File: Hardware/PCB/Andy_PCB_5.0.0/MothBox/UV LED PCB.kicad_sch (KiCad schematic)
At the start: 24 parts, among them P4 External Attractor, Q10 BC817, Q11 BC817, Q8 BC817, Q9 BC817, U10 IRF9335TRPBF, U11 IRF9335TRPBF, U12 IRF9335TRPBF, U13 IRF9335TRPBF

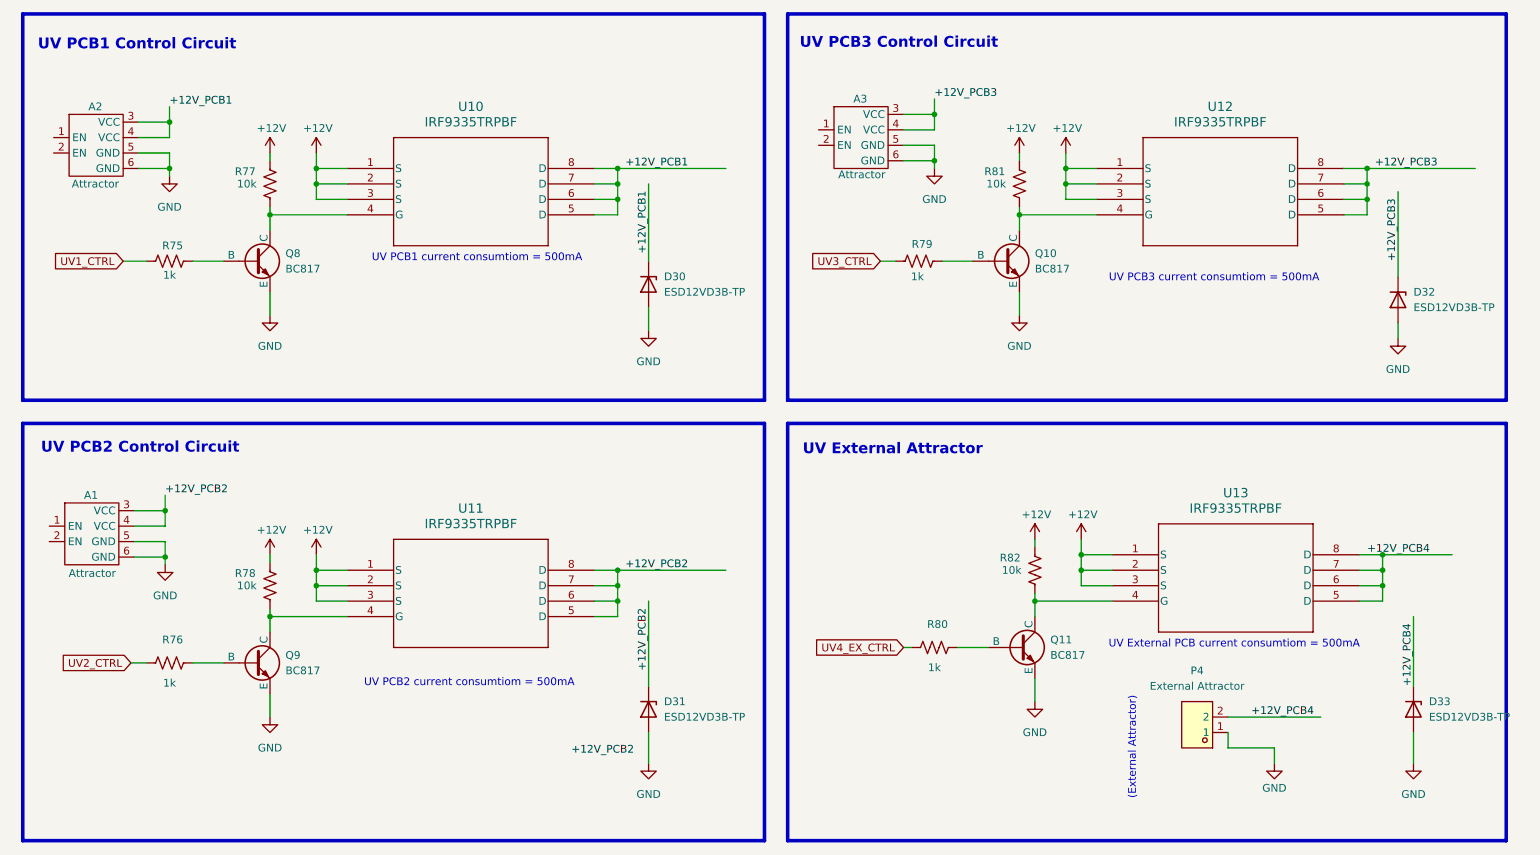
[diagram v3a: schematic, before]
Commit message: Tweaked Mothbeam and added GPS footprints
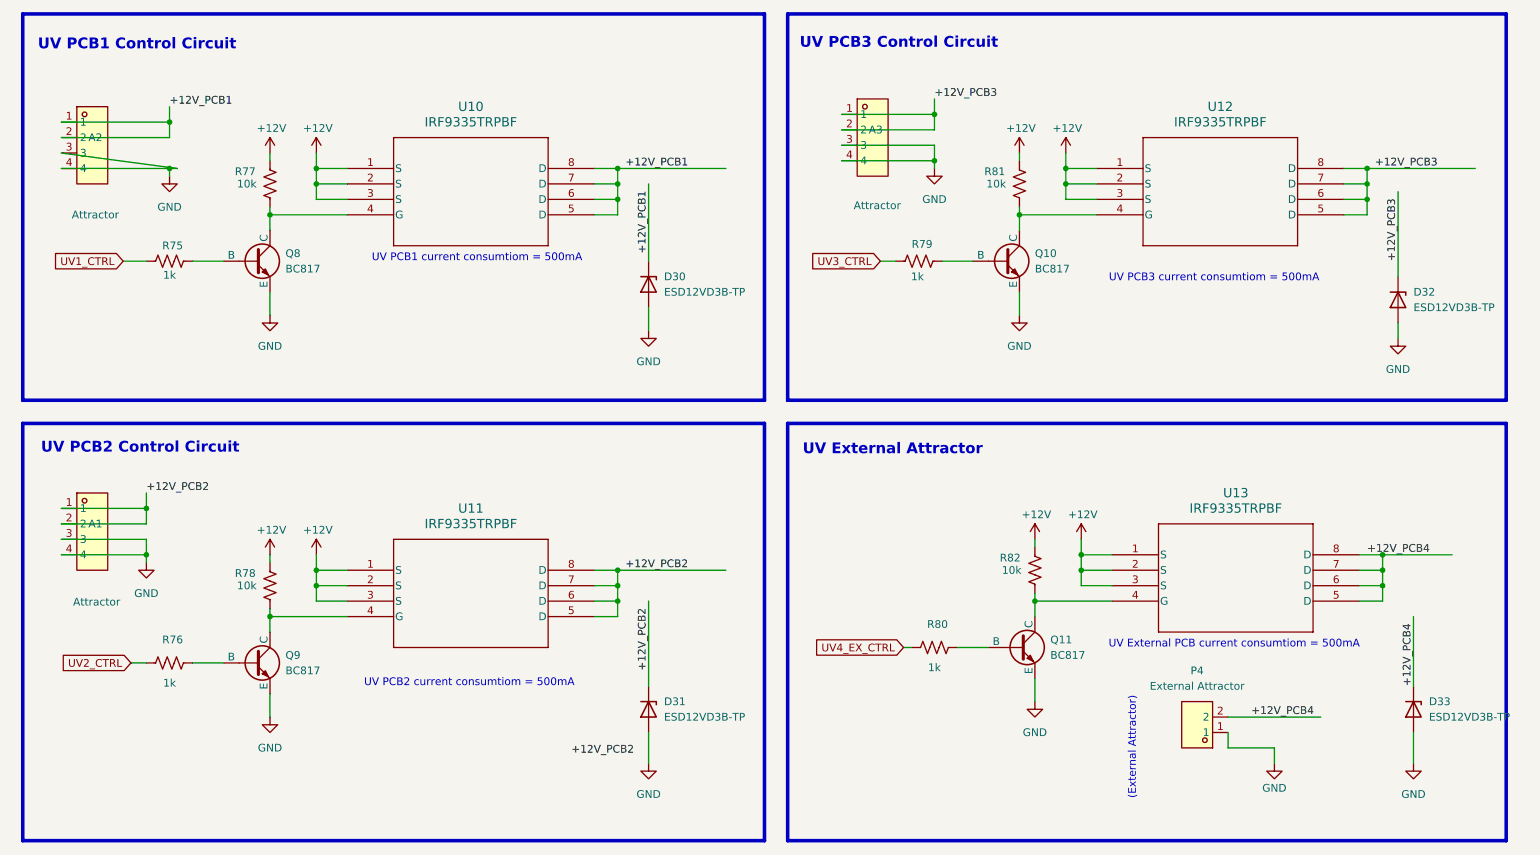
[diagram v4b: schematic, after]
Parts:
- A1, A2, A3: footprint Attractor:attractor -> Attractor:HDR-TH_4P-P2.54-H-M-W10.4; symbol attractor:Attractor_Module -> attractor_AQ:PZ254R-11-04P; LCSC Part (none) -> C492412
- P4: footprint easyeda2kicad:CONN-TH_DB301V-3.5-2P-GN -> easyeda2kicad:CONN-TH_2P-P5.08_DIBO_DB142R-5.08-2P; symbol easyeda2kicad:DB301V-3.5-2P-GN -> easyeda2kicad:DB142R-5.08-2P; LCSC Part C695629 -> C2898709
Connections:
- net +12V_PCB1: now also A2.1, A2.2; no longer A2.3 (VCC), A2.4 (VCC)
- net +12V_PCB2: now also A1.1, A1.2; no longer A1.3 (VCC), A1.4 (VCC)
- net +12V_PCB3: now also A3.1, A3.2; no longer A3.3 (VCC), A3.4 (VCC)
- net GND: now also A1.3, A1.4, A2.3, A2.4, A3.3, A3.4; no longer A1.5 (GND), A1.6 (GND), A2.5 (GND), A2.6 (GND), A3.5 (GND), A3.6 (GND)
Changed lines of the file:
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@@
 	)
 	(junction
-		(at 50.0835 109.5921)
+		(at 46.99 109.22)
 		(diameter 0)
 		(color 0 0 0 0)
@@
 	)
 	(junction
-		(at 50.0835 117.2121)
+		(at 46.99 116.84)
 		(diameter 0)
 		(color 0 0 0 0)
@@
 	(wire
 		(pts
-			(xy 50.0835 117.2121) (xy 50.0835 114.6721)
+			(xy 46.99 116.84) (xy 46.99 114.3)
 		)
 		(stroke
@@
 	(wire
 		(pts
-			(xy 50.0835 107.0521) (xy 50.0835 109.5921)
+			(xy 46.99 106.68) (xy 46.99 109.22)
 		)
 		(stroke
@@
 	(wire
 		(pts
-			(xy 50.0835 118.4821) (xy 50.0835 117.2121)
+			(xy 46.99 118.11) (xy 46.99 116.84)
 		)
 		(stroke
@@
 	(wire
 		(pts
-			(xy 45.0035 109.5921) (xy 50.0835 109.5921)
+			(xy 33.02 109.22) (xy 46.99 109.22)
 		)
 		(stroke
@@
 	(wire
 		(pts
-			(xy 45.0035 117.2121) (xy 50.0835 117.2121)
+			(xy 33.02 116.84) (xy 46.99 116.84)
 		)
 		(stroke
@@
 	(wire
 		(pts
-			(xy 50.0835 112.1321) (xy 50.0835 109.5921)
+			(xy 46.99 111.76) (xy 46.99 109.22)
 		)
 		(stroke
@@
 	(wire
 		(pts
-			(xy 45.72 53.34) (xy 50.8 53.34)
+			(xy 33.02 53.34) (xy 50.8 53.34)
 		)
 		(stroke
@@
 	(wire
 		(pts
-			(xy 171.45 44.45) (xy 176.53 44.45)
+			(xy 161.29 44.45) (xy 176.53 44.45)
 		)
 		(stroke
@@
 	(wire
 		(pts
-			(xy 45.72 45.72) (xy 50.8 45.72)
+			(xy 33.02 45.72) (xy 50.8 45.72)
 		)
 		(stroke
@@
 	(wire
 		(pts
-			(xy 50.8 50.8) (xy 45.72 50.8)
+			(xy 52.07 53.34) (xy 33.02 50.8)
 		)
 		(stroke
@@
 	(wire
 		(pts
-			(xy 50.0835 114.6721) (xy 45.0035 114.6721)
+			(xy 46.99 114.3) (xy 33.02 114.3)
 		)
 		(stroke
@@
 	(wire
 		(pts
-			(xy 171.45 52.07) (xy 176.53 52.07)
+			(xy 161.29 52.07) (xy 176.53 52.07)
 		)
 		(stroke
@@
 	(wire
 		(pts
-			(xy 50.8 53.34) (xy 50.8 50.8)
+			(xy 52.07 53.34) (xy 50.8 53.34)
 		)
 		(stroke
@@
 	(wire
 		(pts
-			(xy 176.53 49.53) (xy 171.45 49.53)
+			(xy 176.53 49.53) (xy 161.29 49.53)
 		)
 		(stroke
@@
 	(wire
 		(pts
-			(xy 45.0035 112.1321) (xy 50.0835 112.1321)
+			(xy 33.02 111.76) (xy 46.99 111.76)
 		)
 		(stroke
@@
 	(wire
 		(pts
-			(xy 45.72 48.26) (xy 50.8 48.26)
+			(xy 33.02 48.26) (xy 50.8 48.26)
 		)
 		(stroke
@@
 	(wire
 		(pts
-			(xy 171.45 46.99) (xy 176.53 46.99)
+			(xy 161.29 46.99) (xy 176.53 46.99)
 		)
 		(stroke
@@
 	)
 	(label "+12V_PCB2"
-		(at 50.0835 107.0521 0)
+		(at 46.99 106.68 0)
 		(effects
 			(font
@@
 	)
 	(symbol
-		(lib_id "easyeda2kicad:DB301V-3.5-2P-GN")
+		(lib_id "easyeda2kicad:DB142R-5.08-2P")
 		(at 219.71 144.78 180)
 		(unit 1)
@@
 			)
 		)
-		(property "Footprint" "easyeda2kicad:CONN-TH_DB301V-3.5-2P-GN"
+		(property "Footprint" "easyeda2kicad:CONN-TH_2P-P5.08_DIBO_DB142R-5.08-2P"
 			(at 219.71 135.89 0)
 			(effects
@@
 		)
 		(property "Datasheet" "https://lcsc.com/product-detail/Wire-To-Board-Wire-To-Wire-Connector_DIBO-DB301V-3-5-2P-GN_C695629.html"
-			(at 219.71 133.35 0)
+			(at 219.71 144.78 0)
 			(effects
 				(font
@@
 			)
 		)
-		(property "LCSC Part" "C695629"
-			(at 219.71 130.81 0)
+		(property "LCSC Part" "C2898709"
+			(at 219.71 133.35 0)
 			(effects
 				(font
@@
 	)
 	(symbol
-		(lib_id "attractor:Attractor_Module")
-		(at 38.1 44.45 0)
+		(lib_id "attractor_AQ:PZ254R-11-04P")
+		(at 38.1 49.53 0)
 		(unit 1)
 		(exclude_from_sim no)
@@
 		(dnp no)
 		(property "Reference" "A2"
-			(at 38.608 43.18 0)
+			(at 38.608 48.26 0)
 			(effects
 				(font
@@
 		)
 		(property "Value" "Attractor"
-			(at 38.608 55.88 0)
+			(at 38.608 60.96 0)
 			(effects
 				(font
@@
 			)
 		)
-		(property "Footprint" "Attractor:attractor"
-			(at 38.1 44.45 0)
+		(property "Footprint" "Attractor:HDR-TH_4P-P2.54-H-M-W10.4"
+			(at 38.1 60.96 0)
 			(effects
 				(font
@@
 			)
 		)
-		(property "Datasheet" ""
-			(at 38.1 44.45 0)
+		(property "Datasheet" "https://lcsc.com/product-detail/Pin-Header-Female-Header_XFCN-PZ254R-11-04P_C492412.html"
+			(at 38.1 63.5 0)
 			(effects
 				(font
@@
 		)
 		(property "Description" ""
-			(at 38.1 44.45 0)
+			(at 38.1 49.53 0)
 			(effects
 				(font
@@
 		)
 		(property "LCSC Part no " "C49661"
-			(at 38.1 44.45 0)
+			(at 38.1 49.53 0)
 			(effects
 				(font
@@
 		)
 		(property "LCSC PN" ""
-			(at 38.1 44.45 0)
+			(at 38.1 49.53 0)
+			(effects
+				(font
+					(size 1.27 1.27)
+				)
+			)
+		)
+		(property "LCSC Part" "C492412"
+			(at 38.1 66.04 0)
 			(effects
 				(font
 					(size 1.27 1.27)
 				)
+				(hide yes)
 			)
 		)
@@
 		(pin "3"
 		)
-		(pin "6"
-		)
 		(pin "2"
 		)
-		(pin "5"
-		)
 		(pin "4"
 		)
@@
 	(symbol
 		(lib_id "power:GND")
-		(at 50.0835 118.4821 0)
+		(at 46.99 118.11 0)
 		(unit 1)
 		(exclude_from_sim no)
@@
 		(fields_autoplaced yes)
 		(property "Reference" "#PWR082"
-			(at 50.0835 124.8321 0)
+			(at 46.99 124.46 0)
 			(effects
 				(font
@@
 		)
 		(property "Value" "GND"
-			(at 50.0835 123.5621 0)
+			(at 46.99 123.19 0)
 			(effects
 				(font
@@
 		)
 		(property "Footprint" ""
-			(at 50.0835 118.4821 0)
+			(at 46.99 118.11 0)
 			(effects
 				(font
@@
 		)
 		(property "Datasheet" ""
-			(at 50.0835 118.4821 0)
+			(at 46.99 118.11 0)
 			(effects
 				(font
@@
 		)
 		(property "Description" "Power symbol creates a global label with name \"GND\" , ground"
-			(at 50.0835 118.4821 0)
+			(at 46.99 118.11 0)
 			(effects
 				(font
@@
 	)
 	(symbol
-		(lib_id "attractor:Attractor_Module")
-		(at 37.3835 108.3221 0)
+		(lib_id "attractor_AQ:PZ254R-11-04P")
+		(at 38.1 113.03 0)
 		(unit 1)
 		(exclude_from_sim no)
@@
 		(dnp no)
 		(property "Reference" "A1"
-			(at 37.8915 107.0521 0)
+			(at 38.608 111.76 0)
 			(effects
 				(font
@@
 		)
 		(property "Value" "Attractor"
-			(at 38.1 119.888 0)
+			(at 38.8165 124.5959 0)
 			(effects
 				(font
@@
 			)
 		)
-		(property "Footprint" "Attractor:attractor"
-			(at 37.3835 108.3221 0)
+		(property "Footprint" "Attractor:HDR-TH_4P-P2.54-H-M-W10.4"
+			(at 38.1 124.46 0)
 			(effects
 				(font
@@
 			)
 		)
-		(property "Datasheet" ""
-			(at 37.3835 108.3221 0)
+		(property "Datasheet" "https://lcsc.com/product-detail/Pin-Header-Female-Header_XFCN-PZ254R-11-04P_C492412.html"
+			(at 38.1 127 0)
 			(effects
 				(font
@@
 		)
 		(property "Description" ""
-			(at 37.3835 108.3221 0)
+			(at 38.1 113.03 0)
 			(effects
 				(font
@@
 		)
 		(property "LCSC Part no " "C49661"
-			(at 37.3835 108.3221 0)
+			(at 38.1 113.03 0)
 			(effects
 				(font
@@
 		)
 		(property "LCSC PN" ""
-			(at 37.3835 108.3221 0)
+			(at 38.1 113.03 0)
 			(effects
 				(font
@@
 			)
 		)
+		(property "LCSC Part" "C492412"
+			(at 38.1 129.54 0)
+			(effects
+				(font
+					(size 1.27 1.27)
+				)
+				(hide yes)
+			)
+		)
 		(pin "1"
 		)
 		(pin "3"
 		)
-		(pin "6"
-		)
 		(pin "2"
 		)
-		(pin "5"
-		)
 		(pin "4"
 		)
@@
 	)
 	(symbol
-		(lib_id "attractor:Attractor_Module")
-		(at 163.83 43.18 0)
+		(lib_id "attractor_AQ:PZ254R-11-04P")
+		(at 166.37 48.26 0)
 		(unit 1)
 		(exclude_from_sim no)
@@
 		(dnp no)
 		(property "Reference" "A3"
-			(at 164.338 41.91 0)
+			(at 166.878 46.99 0)
 			(effects
 				(font
@@
 		)
 		(property "Value" "Attractor"
-			(at 164.592 54.356 0)
+			(at 167.132 59.436 0)
 			(effects
 				(font
@@
 			)
 		)
-		(property "Footprint" "Attractor:attractor"
-			(at 163.83 43.18 0)
+		(property "Footprint" "Attractor:HDR-TH_4P-P2.54-H-M-W10.4"
+			(at 166.37 59.69 0)
 			(effects
 				(font
@@
 			)
 		)
-		(property "Datasheet" ""
-			(at 163.83 43.18 0)
+		(property "Datasheet" "https://lcsc.com/product-detail/Pin-Header-Female-Header_XFCN-PZ254R-11-04P_C492412.html"
+			(at 166.37 62.23 0)
 			(effects
 				(font
@@
 		)
 		(property "Description" ""
-			(at 163.83 43.18 0)
+			(at 166.37 48.26 0)
 			(effects
 				(font
@@
 		)
 		(property "LCSC Part no " "C49661"
-			(at 163.83 43.18 0)
+			(at 166.37 48.26 0)
 			(effects
 				(font
@@
 		)
 		(property "LCSC PN" ""
-			(at 163.83 43.18 0)
+			(at 166.37 48.26 0)
 			(effects
 				(font
@@
 			)
 		)
+		(property "LCSC Part" "C492412"
+			(at 166.37 64.77 0)
+			(effects
+				(font
+					(size 1.27 1.27)
+				)
+				(hide yes)
+			)
+		)
 		(pin "1"
 		)
 		(pin "3"
 		)
-		(pin "6"
-		)
 		(pin "2"
 		)
-		(pin "5"
-		)
 		(pin "4"

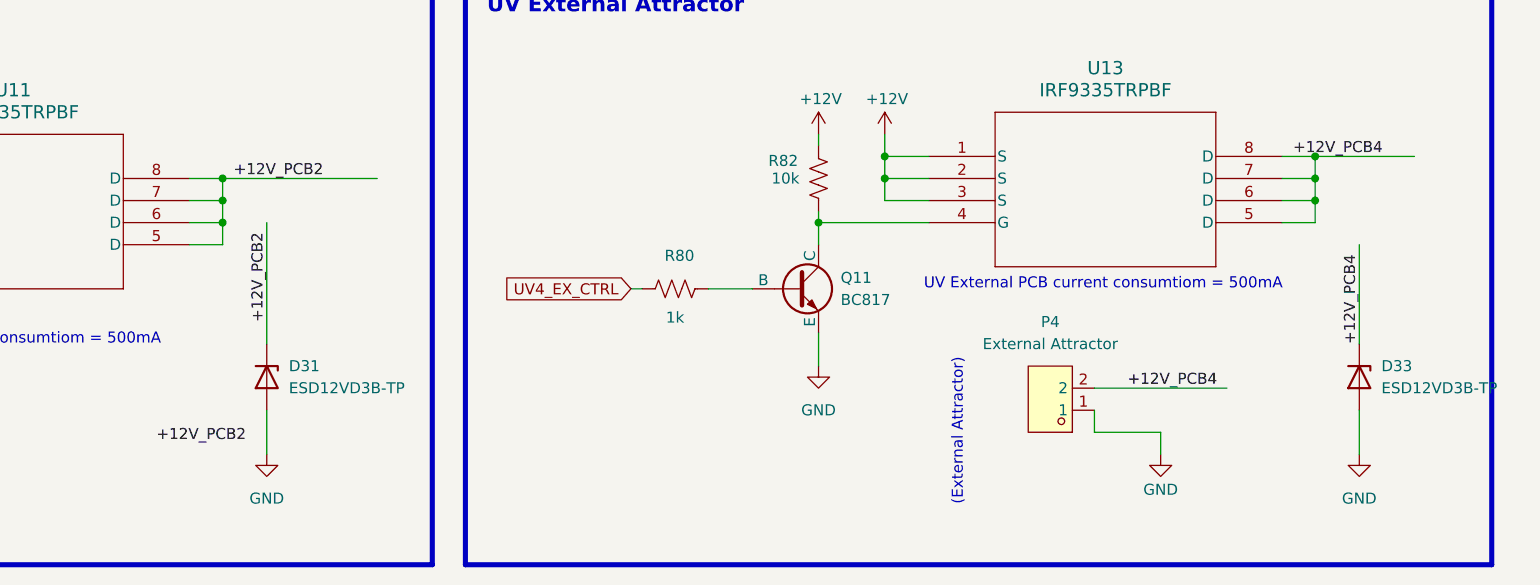
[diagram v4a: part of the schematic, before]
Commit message: cleaned most schematic and got rid of half errors in ERC
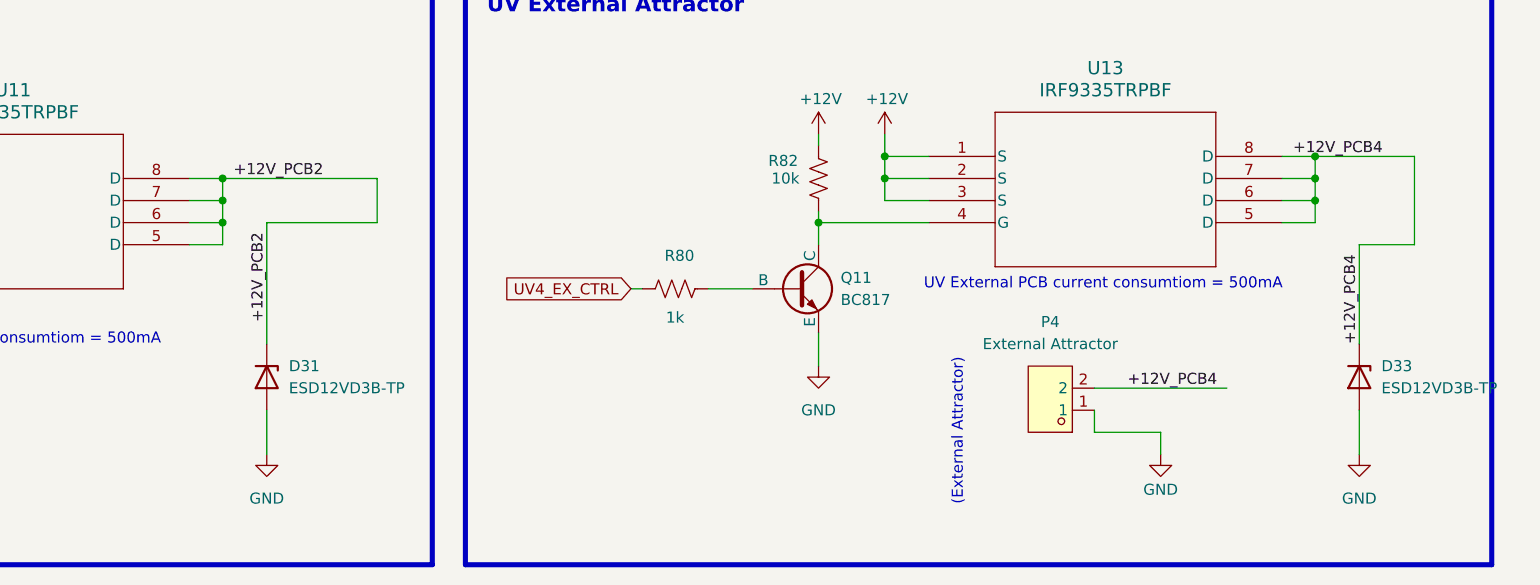
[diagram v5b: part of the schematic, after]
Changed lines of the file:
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@@
+	(wire
+		(pts
+			(xy 142.24 124.46) (xy 129.54 124.46)
+		)
+		(stroke
+			(width 0)
+			(type default)
+		)
+	)
 	(wire
 		(pts
@@
 	(wire
 		(pts
+			(xy 142.24 119.38) (xy 142.24 124.46)
+		)
+		(stroke
+			(width 0)
+			(type default)
+		)
+	)
+	(wire
+		(pts
 			(xy 246.38 121.92) (xy 250.19 121.92)
 		)
@@
 	(wire
 		(pts
+			(xy 261.62 127) (xy 255.27 127)
+		)
+		(stroke
+			(width 0)
+			(type default)
+		)
+	)
+	(wire
+		(pts
 			(xy 200.66 119.38) (xy 200.66 116.84)
 		)
@@
 		(pts
 			(xy 171.45 132.08) (xy 172.72 132.08)
+		)
+		(stroke
+			(width 0)
+			(type default)
+		)
+	)
+	(wire
+		(pts
+			(xy 261.62 116.84) (xy 261.62 127)
 		)
 		(stroke
@@
 		(effects
 			(font
-				(size 1.27 1.27)
-			)
-			(justify left bottom)
-		)
-	)
-	(label "+12V_PCB2"
-		(at 116.84 149.86 0)
-		(effects
-			(font
